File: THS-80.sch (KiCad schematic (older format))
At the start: 20 parts, among them J1 USB_B_Micro, J2 RC80 Bus, J3 RC80 Expansion, SW1 Reset, U1 MAX40203AUK, U2 DS1813R-5+T&R

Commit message: layout changes, silkscreen fixes
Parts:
- renumbered C2 to C1, C22 to C2, C23 to C4, C1 to C5, C25 to C6, C31 to C7, D15 to D1, R42 to R2, R2 to R3, R3 to R4, R4 to R5, R5 to R6
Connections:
- net labels added: VCC
- net labels removed: +5V

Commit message: changes
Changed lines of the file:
@@
 Wire Bus Line
 	7350 900  6700 900
-$Comp
-L Device:R_Small R6
-U 1 1 5F3BDAB6
-P 6030 4000
-AR Path="/5F3BDAB6" Ref="R6"  Part="1"
-AR Path="/5D6224DC/5F3BDAB6" Ref="R?"  Part="1"
-F 0 "R6" V 5955 3925 50  0000 L CNN
-F 1 "10K" V 6030 3950 32  0000 L CNN
-F 2 "Resistor_SMD:R_0603_1608Metric_Pad1.05x0.95mm_HandSolder" H 6030 4000 50  0001 C CNN
-F 3 "~" H 6030 4000 50  0001 C CNN
-	1    6030 4000
-	1    0    0    -1
-$EndComp
-$Comp
-L Device:R_Small R5
-U 1 1 5F3BDABC
-P 5880 4000
-AR Path="/5F3BDABC" Ref="R5"  Part="1"
-AR Path="/5D6224DC/5F3BDABC" Ref="R?"  Part="1"
-F 0 "R5" V 5805 3925 50  0000 L CNN
-F 1 "10K" V 5880 3950 32  0000 L CNN
-F 2 "Resistor_SMD:R_0603_1608Metric_Pad1.05x0.95mm_HandSolder" H 5880 4000 50  0001 C CNN
-F 3 "~" H 5880 4000 50  0001 C CNN
-	1    5880 4000
-	1    0    0    -1
-$EndComp
-$Comp
-L Device:R_Small R4
-U 1 1 5F3BDAC2
-P 5730 4000
-AR Path="/5F3BDAC2" Ref="R4"  Part="1"
-AR Path="/5D6224DC/5F3BDAC2" Ref="R?"  Part="1"
-F 0 "R4" V 5655 3925 50  0000 L CNN
-F 1 "10K" V 5730 3950 32  0000 L CNN
-F 2 "Resistor_SMD:R_0603_1608Metric_Pad1.05x0.95mm_HandSolder" H 5730 4000 50  0001 C CNN
-F 3 "~" H 5730 4000 50  0001 C CNN
-	1    5730 4000
-	1    0    0    -1
-$EndComp
-$Comp
-L Device:R_Small R3
-U 1 1 5F3BDAC8
-P 5580 4000
-AR Path="/5F3BDAC8" Ref="R3"  Part="1"
-AR Path="/5D6224DC/5F3BDAC8" Ref="R?"  Part="1"
-F 0 "R3" V 5505 3925 50  0000 L CNN
-F 1 "10K" V 5580 3950 32  0000 L CNN
-F 2 "Resistor_SMD:R_0603_1608Metric_Pad1.05x0.95mm_HandSolder" H 5580 4000 50  0001 C CNN
-F 3 "~" H 5580 4000 50  0001 C CNN
-	1    5580 4000
-	1    0    0    -1
-$EndComp
-Wire Wire Line
-	5580 3900 5580 3800
-Wire Wire Line
-	5580 3800 5730 3800
-Wire Wire Line
-	6030 3800 6030 3900
-Wire Wire Line
-	5880 3900 5880 3800
-Connection ~ 5880 3800
-Wire Wire Line
-	5880 3800 6030 3800
-Wire Wire Line
-	5730 3900 5730 3800
-Connection ~ 5730 3800
-Wire Wire Line
-	6030 4100 6030 4450
-Text Label 6030 4150 3    50   ~ 0
-~BUSRQ
-Text Label 5880 4200 3    50   ~ 0
-~WAIT
-Text Label 5730 4200 3    50   ~ 0
-~NMI
-Text Label 5580 4300 1    50   ~ 0
-~INT
-Wire Wire Line
-	5880 4100 5880 4450
-Wire Wire Line
-	5730 4100 5730 4450
-Wire Wire Line
-	5580 4100 5580 4450
-Text Label 6350 5600 0    50   ~ 0
-~RESET
-Wire Wire Line
-	5600 6000 6200 6000
-Wire Wire Line
-	6000 5600 6200 5600
-Connection ~ 6200 5600
-Connection ~ 5600 6000
-$Comp
-L THS-80:DS1813R-5+T&R U2
-U 1 1 5F3E91F7
-P 5700 5600
-AR Path="/5F3E91F7" Ref="U2"  Part="1"
-AR Path="/5D6224DC/5F3E91F7" Ref="U?"  Part="1"
-F 0 "U2" H 5470 5646 50  0000 R CNN
-F 1 "DS1813R-5+T&R" H 6350 5950 50  0000 R CNN
-F 2 "Package_TO_SOT_SMD:SOT-23" H 5300 5750 50  0001 C CNN
-F 3 "https://www.mouser.com/datasheet/2/256/maxim%20integrated%20products_ds1813-1178753.pdf" H 5400 5850 50  0001 C CNN
-	1    5700 5600
-	1    0    0    -1
-$EndComp
-$Comp
-L Switch:SW_Push SW1
-U 1 1 5F3E91FD
-P 6200 5800
-AR Path="/5F3E91FD" Ref="SW1"  Part="1"
-AR Path="/5D6224DC/5F3E91FD" Ref="SW?"  Part="1"
-F 0 "SW1" V 6154 5948 50  0000 L CNN
-F 1 "Reset" V 6245 5948 50  0000 L CNN
-F 2 "Button_Switch_SMD:SW_SPST_FSMSM" H 6200 6000 50  0001 C CNN
-F 3 "~" H 6200 6000 50  0001 C CNN
-	1    6200 5800
-	0    1    1    0
-$EndComp
-Wire Wire Line
-	6200 5600 6650 5600
-$Comp
-L power:GND #PWR014
-U 1 1 5F3E920A
-P 5600 6100
-AR Path="/5F3E920A" Ref="#PWR014"  Part="1"
-AR Path="/5CB63856/5F3E920A" Ref="#PWR?"  Part="1"
-AR Path="/5CB5AB00/5CB63856/5F3E920A" Ref="#PWR?"  Part="1"
-AR Path="/5CFABACD/5F3E920A" Ref="#PWR?"  Part="1"
-AR Path="/5CF9C1ED/5F3E920A" Ref="#PWR?"  Part="1"
-AR Path="/5D6224DC/5F3E920A" Ref="#PWR?"  Part="1"
-F 0 "#PWR014" H 5600 5850 50  0001 C CNN
-F 1 "GND" H 5604 5958 50  0000 C CNN
-F 2 "" H 5600 6100 50  0001 C CNN
-F 3 "" H 5600 6100 50  0001 C CNN
-	1    5600 6100
-	1    0    0    -1
-$EndComp
-Wire Wire Line
-	5600 6000 5600 6100
 Text Label 10025 1950 2    50   ~ 0
 ~INT
@@
 Wire Wire Line
 	1350 2250 1050 2250
-Wire Wire Line
-	5730 3800 5800 3800
-Wire Wire Line
-	5800 3700 5800 3800
-Connection ~ 5800 3800
-Wire Wire Line
-	5800 3800 5880 3800
 $Comp
 L power:PWR_FLAG #FLG01
@@
 $EndComp
 $Comp
-L power:VCC #PWR0104
-U 1 1 5DBFDEF7
-P 5600 5200
-F 0 "#PWR0104" H 5600 5050 50  0001 C CNN
-F 1 "VCC" H 5617 5373 50  0000 C CNN
-F 2 "" H 5600 5200 50  0001 C CNN
-F 3 "" H 5600 5200 50  0001 C CNN
-	1    5600 5200
-	1    0    0    -1
-$EndComp
-$Comp
-L power:VCC #PWR0105
-U 1 1 5DC183D7
-P 5800 3700
-F 0 "#PWR0105" H 5800 3550 50  0001 C CNN
-F 1 "VCC" H 5817 3873 50  0000 C CNN
-F 2 "" H 5800 3700 50  0001 C CNN
-F 3 "" H 5800 3700 50  0001 C CNN
-	1    5800 3700
-	1    0    0    -1
-$EndComp
-$Comp
 L power:VCC #PWR0136
 U 1 1 5DFA88CB
@@
 	1    0    0    -1
 $EndComp
+$Comp
+L Device:R_Small R6
+U 1 1 5E47A0BC
+P 6280 3550
+AR Path="/5E47A0BC" Ref="R6"  Part="1"
+AR Path="/5D6224DC/5E47A0BC" Ref="R?"  Part="1"
+F 0 "R6" V 6205 3475 50  0000 L CNN
+F 1 "10K" V 6280 3500 32  0000 L CNN
+F 2 "Resistor_SMD:R_0603_1608Metric_Pad1.05x0.95mm_HandSolder" H 6280 3550 50  0001 C CNN
+F 3 "~" H 6280 3550 50  0001 C CNN
+	1    6280 3550
+	1    0    0    -1
+$EndComp
+$Comp
+L Device:R_Small R5
+U 1 1 5E47A0C2
+P 6130 3550
+AR Path="/5E47A0C2" Ref="R5"  Part="1"
+AR Path="/5D6224DC/5E47A0C2" Ref="R?"  Part="1"
+F 0 "R5" V 6055 3475 50  0000 L CNN
+F 1 "10K" V 6130 3500 32  0000 L CNN
+F 2 "Resistor_SMD:R_0603_1608Metric_Pad1.05x0.95mm_HandSolder" H 6130 3550 50  0001 C CNN
+F 3 "~" H 6130 3550 50  0001 C CNN
+	1    6130 3550
+	1    0    0    -1
+$EndComp
+$Comp
+L Device:R_Small R4
+U 1 1 5E47A0C8
+P 5980 3550
+AR Path="/5E47A0C8" Ref="R4"  Part="1"
+AR Path="/5D6224DC/5E47A0C8" Ref="R?"  Part="1"
+F 0 "R4" V 5905 3475 50  0000 L CNN
+F 1 "10K" V 5980 3500 32  0000 L CNN
+F 2 "Resistor_SMD:R_0603_1608Metric_Pad1.05x0.95mm_HandSolder" H 5980 3550 50  0001 C CNN
+F 3 "~" H 5980 3550 50  0001 C CNN
+	1    5980 3550
+	1    0    0    -1
+$EndComp
+$Comp
+L Device:R_Small R3
+U 1 1 5E47A0CE
+P 5830 3550
+AR Path="/5E47A0CE" Ref="R3"  Part="1"
+AR Path="/5D6224DC/5E47A0CE" Ref="R?"  Part="1"
+F 0 "R3" V 5755 3475 50  0000 L CNN
+F 1 "10K" V 5830 3500 32  0000 L CNN
+F 2 "Resistor_SMD:R_0603_1608Metric_Pad1.05x0.95mm_HandSolder" H 5830 3550 50  0001 C CNN
+F 3 "~" H 5830 3550 50  0001 C CNN
+	1    5830 3550
+	1    0    0    -1
+$EndComp
+Wire Wire Line
+	5830 3450 5830 3350
+Wire Wire Line
+	5830 3350 5980 3350
+Wire Wire Line
+	6280 3350 6280 3450
+Wire Wire Line
+	6130 3450 6130 3350
+Connection ~ 6130 3350
+Wire Wire Line
+	6130 3350 6280 3350
+Wire Wire Line
+	5980 3450 5980 3350
+Connection ~ 5980 3350
+Wire Wire Line
+	6280 3650 6280 4000
+Text Label 6280 3700 3    50   ~ 0
+~BUSRQ
+Text Label 6130 3750 3    50   ~ 0
+~WAIT
+Text Label 5980 3750 3    50   ~ 0
+~NMI
+Text Label 5830 3850 1    50   ~ 0
+~INT
+Wire Wire Line
+	6130 3650 6130 4000
+Wire Wire Line
+	5980 3650 5980 4000
+Wire Wire Line
+	5830 3650 5830 4000
+Text Label 6600 5150 0    50   ~ 0
+~RESET
+Wire Wire Line
+	5850 5550 6450 5550
+Wire Wire Line
+	6250 5150 6450 5150
+Connection ~ 6450 5150
+Connection ~ 5850 5550
+$Comp
+L THS-80:DS1813R-5+T&R U2
+U 1 1 5E47A0E9
+P 5950 5150
+AR Path="/5E47A0E9" Ref="U2"  Part="1"
+AR Path="/5D6224DC/5E47A0E9" Ref="U?"  Part="1"
+F 0 "U2" H 5720 5196 50  0000 R CNN
+F 1 "DS1813R-5+T&R" H 6600 5500 50  0000 R CNN
+F 2 "Package_TO_SOT_SMD:SOT-23" H 5550 5300 50  0001 C CNN
+F 3 "https://www.mouser.com/datasheet/2/256/maxim%20integrated%20products_ds1813-1178753.pdf" H 5650 5400 50  0001 C CNN
+	1    5950 5150
+	1    0    0    -1
+$EndComp
+$Comp
+L Switch:SW_Push SW1
+U 1 1 5E47A0EF
+P 6450 5350
+AR Path="/5E47A0EF" Ref="SW1"  Part="1"
+AR Path="/5D6224DC/5E47A0EF" Ref="SW?"  Part="1"
+F 0 "SW1" V 6404 5498 50  0000 L CNN
+F 1 "Reset" V 6495 5498 50  0000 L CNN
+F 2 "Button_Switch_SMD:SW_SPST_FSMSM" H 6450 5550 50  0001 C CNN
+F 3 "~" H 6450 5550 50  0001 C CNN
+	1    6450 5350
+	0    1    1    0
+$EndComp
+Wire Wire Line
+	6450 5150 6900 5150
+$Comp
+L power:GND #PWR0104
+U 1 1 5E47A0F6
+P 5850 5650
+AR Path="/5E47A0F6" Ref="#PWR0104"  Part="1"
+AR Path="/5CB63856/5E47A0F6" Ref="#PWR?"  Part="1"
+AR Path="/5CB5AB00/5CB63856/5E47A0F6" Ref="#PWR?"  Part="1"
+AR Path="/5CFABACD/5E47A0F6" Ref="#PWR?"  Part="1"
+AR Path="/5CF9C1ED/5E47A0F6" Ref="#PWR?"  Part="1"
+AR Path="/5D6224DC/5E47A0F6" Ref="#PWR?"  Part="1"
+F 0 "#PWR0104" H 5850 5400 50  0001 C CNN
+F 1 "GND" H 5854 5508 50  0000 C CNN
+F 2 "" H 5850 5650 50  0001 C CNN
+F 3 "" H 5850 5650 50  0001 C CNN
+	1    5850 5650
+	1    0    0    -1
+$EndComp
+Wire Wire Line
+	5850 5550 5850 5650
+Wire Wire Line
+	5980 3350 6050 3350
+Wire Wire Line
+	6050 3250 6050 3350
+Connection ~ 6050 3350
+Wire Wire Line
+	6050 3350 6130 3350
+$Comp
+L power:VCC #PWR0105
+U 1 1 5E47A101
+P 5850 4750
+F 0 "#PWR0105" H 5850 4600 50  0001 C CNN
+F 1 "VCC" H 5867 4923 50  0000 C CNN
+F 2 "" H 5850 4750 50  0001 C CNN
+F 3 "" H 5850 4750 50  0001 C CNN
+	1    5850 4750
+	1    0    0    -1
+$EndComp
+$Comp
+L power:VCC #PWR0137
+U 1 1 5E47A107
+P 6050 3250
+F 0 "#PWR0137" H 6050 3100 50  0001 C CNN
+F 1 "VCC" H 6067 3423 50  0000 C CNN
+F 2 "" H 6050 3250 50  0001 C CNN
+F 3 "" H 6050 3250 50  0001 C CNN
+	1    6050 3250
+	1    0    0    -1
+$EndComp

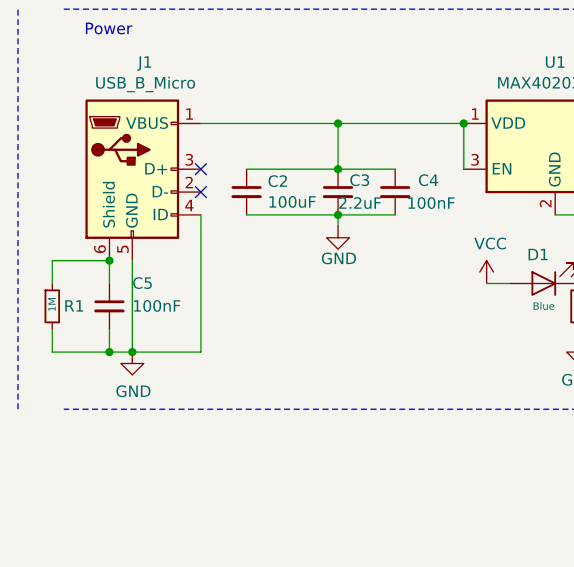
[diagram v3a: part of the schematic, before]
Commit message: gnd plane fixes
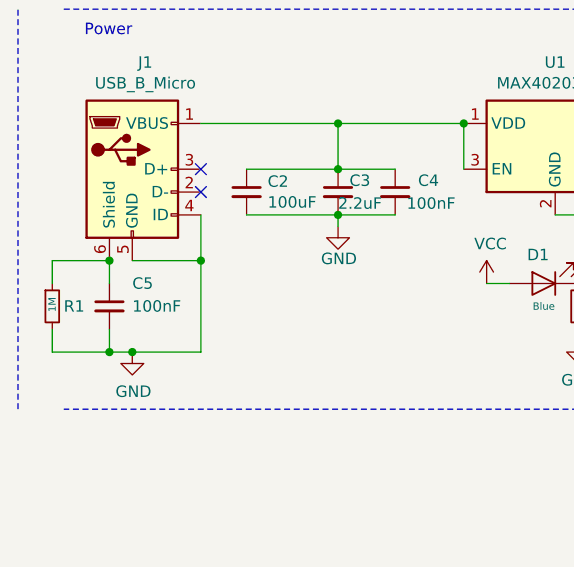
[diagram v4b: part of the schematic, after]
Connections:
- wire segments 250 -> 251
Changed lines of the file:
@@
 Connection ~ 950  2250
 Wire Wire Line
-	1050 1850 1050 2250
-Wire Wire Line
-	1350 1650 1350 2250
+	1350 1650 1350 1850
 Wire Wire Line
 	1350 2250 1050 2250
@@
 	1    0    0    -1
 $EndComp
+Wire Wire Line
+	1050 1850 1350 1850
+Connection ~ 1350 1850
+Wire Wire Line
+	1350 1850 1350 2250
 $EndSCHEMATC

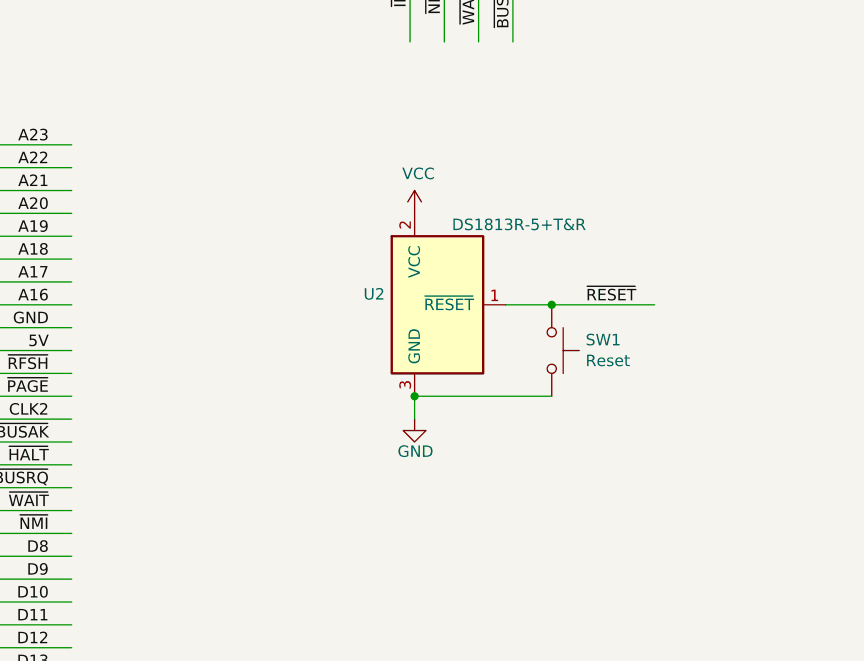
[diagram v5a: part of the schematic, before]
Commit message: Added reset and rom write ena jumpers
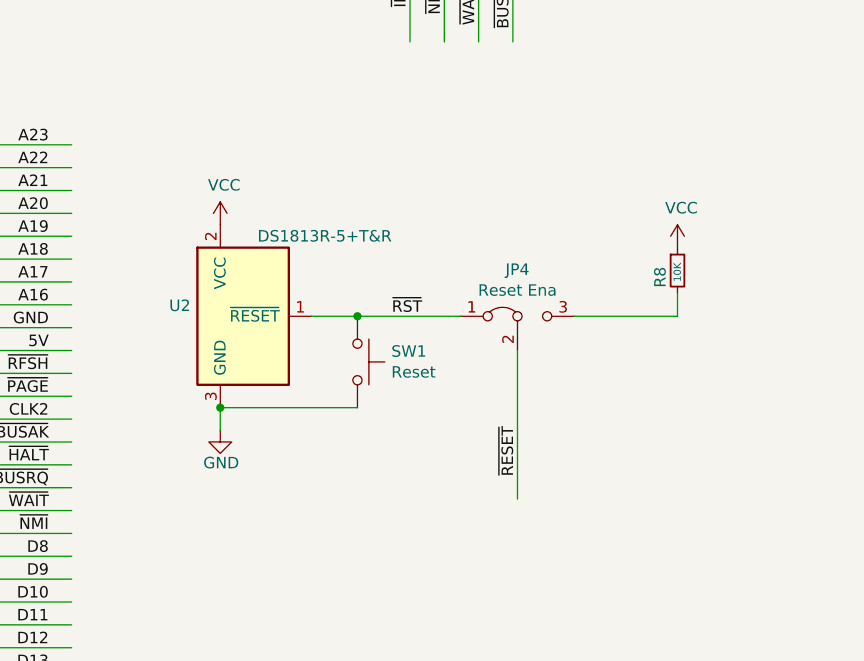
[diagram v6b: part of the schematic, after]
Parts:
- added JP4: Reset Ena, Connector_PinHeader_2.54mm:PinHeader_1x03_P2.54mm_Vertical, symbol Jumper:Jumper_3_Bridged12
- added R8: 10K, Resistor_SMD:R_0603_1608Metric_Pad1.05x0.95mm_HandSolder, symbol Device:R_Small
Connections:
- net labels added: ~RST
- wire segments 251 -> 254
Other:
- moved on the sheet: SW1, U2
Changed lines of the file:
@@
 Wire Wire Line
 	5830 3650 5830 4000
-Text Label 6600 5150 0    50   ~ 0
-~RESET
+Text Label 5750 5200 0    50   ~ 0
+~RST
 Wire Wire Line
-	5850 5550 6450 5550
+	5000 5600 5600 5600
 Wire Wire Line
-	6250 5150 6450 5150
-Connection ~ 6450 5150
-Connection ~ 5850 5550
+	5400 5200 5600 5200
+Connection ~ 5600 5200
+Connection ~ 5000 5600
 $Comp
 L THS-80:DS1813R-5+T&R U2
 U 1 1 5E47A0E9
-P 5950 5150
+P 5100 5200
 AR Path="/5E47A0E9" Ref="U2"  Part="1"
 AR Path="/5D6224DC/5E47A0E9" Ref="U?"  Part="1"
-F 0 "U2" H 5720 5196 50  0000 R CNN
-F 1 "DS1813R-5+T&R" H 6600 5500 50  0000 R CNN
-F 2 "Package_TO_SOT_SMD:SOT-23" H 5550 5300 50  0001 C CNN
-F 3 "https://www.mouser.com/datasheet/2/256/maxim%20integrated%20products_ds1813-1178753.pdf" H 5650 5400 50  0001 C CNN
-	1    5950 5150
+F 0 "U2" H 4870 5246 50  0000 R CNN
+F 1 "DS1813R-5+T&R" H 5750 5550 50  0000 R CNN
+F 2 "Package_TO_SOT_SMD:SOT-23" H 4700 5350 50  0001 C CNN
+F 3 "https://www.mouser.com/datasheet/2/256/maxim%20integrated%20products_ds1813-1178753.pdf" H 4800 5450 50  0001 C CNN
+	1    5100 5200
 	1    0    0    -1
 $EndComp
@@
 L Switch:SW_Push SW1
 U 1 1 5E47A0EF
-P 6450 5350
+P 5600 5400
 AR Path="/5E47A0EF" Ref="SW1"  Part="1"
 AR Path="/5D6224DC/5E47A0EF" Ref="SW?"  Part="1"
-F 0 "SW1" V 6404 5498 50  0000 L CNN
-F 1 "Reset" V 6495 5498 50  0000 L CNN
-F 2 "Button_Switch_SMD:SW_SPST_FSMSM" H 6450 5550 50  0001 C CNN
-F 3 "~" H 6450 5550 50  0001 C CNN
-	1    6450 5350
+F 0 "SW1" V 5554 5548 50  0000 L CNN
+F 1 "Reset" V 5645 5548 50  0000 L CNN
+F 2 "Button_Switch_SMD:SW_SPST_FSMSM" H 5600 5600 50  0001 C CNN
+F 3 "~" H 5600 5600 50  0001 C CNN
+	1    5600 5400
 	0    1    1    0
 $EndComp
 Wire Wire Line
-	6450 5150 6900 5150
+	5600 5200 6050 5200
 $Comp
 L power:GND #PWR0104
 U 1 1 5E47A0F6
-P 5850 5650
+P 5000 5700
 AR Path="/5E47A0F6" Ref="#PWR0104"  Part="1"
 AR Path="/5CB63856/5E47A0F6" Ref="#PWR?"  Part="1"
@@
 AR Path="/5CF9C1ED/5E47A0F6" Ref="#PWR?"  Part="1"
 AR Path="/5D6224DC/5E47A0F6" Ref="#PWR?"  Part="1"
-F 0 "#PWR0104" H 5850 5400 50  0001 C CNN
-F 1 "GND" H 5854 5508 50  0000 C CNN
-F 2 "" H 5850 5650 50  0001 C CNN
-F 3 "" H 5850 5650 50  0001 C CNN
-	1    5850 5650
+F 0 "#PWR0104" H 5000 5450 50  0001 C CNN
+F 1 "GND" H 5004 5558 50  0000 C CNN
+F 2 "" H 5000 5700 50  0001 C CNN
+F 3 "" H 5000 5700 50  0001 C CNN
+	1    5000 5700
 	1    0    0    -1
 $EndComp
 Wire Wire Line
-	5850 5550 5850 5650
+	5000 5600 5000 5700
 Wire Wire Line
 	5980 3350 6050 3350
@@
 L power:VCC #PWR0105
 U 1 1 5E47A101
-P 5850 4750
-F 0 "#PWR0105" H 5850 4600 50  0001 C CNN
-F 1 "VCC" H 5867 4923 50  0000 C CNN
-F 2 "" H 5850 4750 50  0001 C CNN
-F 3 "" H 5850 4750 50  0001 C CNN
-	1    5850 4750
+P 5000 4800
+F 0 "#PWR0105" H 5000 4650 50  0001 C CNN
+F 1 "VCC" H 5017 4973 50  0000 C CNN
+F 2 "" H 5000 4800 50  0001 C CNN
+F 3 "" H 5000 4800 50  0001 C CNN
+	1    5000 4800
 	1    0    0    -1
 $EndComp
@@
 Wire Wire Line
 	1350 1850 1350 2250
+$Comp
+L Jumper:Jumper_3_Bridged12 JP4
+U 1 1 5E93CDF4
+P 6300 5200
+F 0 "JP4" H 6300 5404 50  0000 C CNN
+F 1 "Reset Ena" H 6300 5313 50  0000 C CNN
+F 2 "Connector_PinHeader_2.54mm:PinHeader_1x03_P2.54mm_Vertical" H 6300 5200 50  0001 C CNN
+F 3 "~" H 6300 5200 50  0001 C CNN
+	1    6300 5200
+	1    0    0    -1
+$EndComp
+Text Label 6300 5900 1    50   ~ 0
+~RESET
+Wire Wire Line
+	6300 5350 6300 6000
+Wire Wire Line
+	6550 5200 7000 5200
+$Comp
+L Device:R_Small R8
+U 1 1 5E975106
+P 7000 5000
+AR Path="/5E975106" Ref="R8"  Part="1"
+AR Path="/5D6224DC/5E975106" Ref="R?"  Part="1"
+F 0 "R8" V 6925 4925 50  0000 L CNN
+F 1 "10K" V 7000 4950 32  0000 L CNN
+F 2 "Resistor_SMD:R_0603_1608Metric_Pad1.05x0.95mm_HandSolder" H 7000 5000 50  0001 C CNN
+F 3 "~" H 7000 5000 50  0001 C CNN
+	1    7000 5000
+	1    0    0    -1
+$EndComp
+$Comp
+L power:VCC #PWR0139
+U 1 1 5E9FD853
+P 7000 4900
+F 0 "#PWR0139" H 7000 4750 50  0001 C CNN
+F 1 "VCC" H 7017 5073 50  0000 C CNN
+F 2 "" H 7000 4900 50  0001 C CNN
+F 3 "" H 7000 4900 50  0001 C CNN
+	1    7000 4900
+	1    0    0    -1
+$EndComp
+Wire Wire Line
+	7000 5100 7000 5200
 $EndSCHEMATC
